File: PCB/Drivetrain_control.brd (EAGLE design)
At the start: 94 x 109.9 mm, 49 parts, among them IC1 LM358N, J1 SSW-110-02-G-S, J2 SSW-110-02-G-S, J3 SSW-110-02-G-S, J4 SSW-110-02-G-S, J5 SSW-110-02-G-S, J6 SSW-110-02-G-S, J7 SSW-110-02-G-S, J8 SSW-110-02-G-S, Q1 220mA/50V/3.5Ω, Q10 100V/17A, Q2 100V/17A, Q6 100V/17A, Q7 100V/17A, Q8 100V/17A, Q9 100V/17A

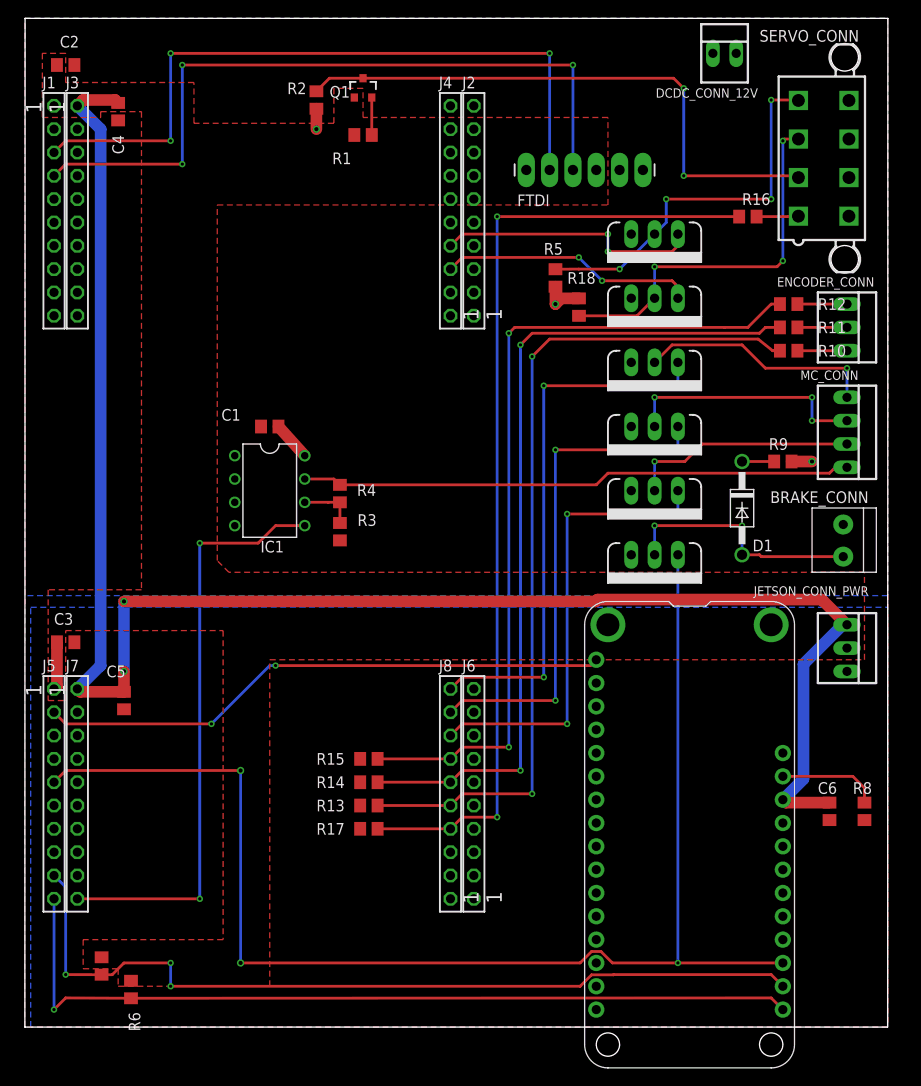
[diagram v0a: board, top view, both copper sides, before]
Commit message: Changed Size now, 100mm x 100mm, Stil Version 1.0
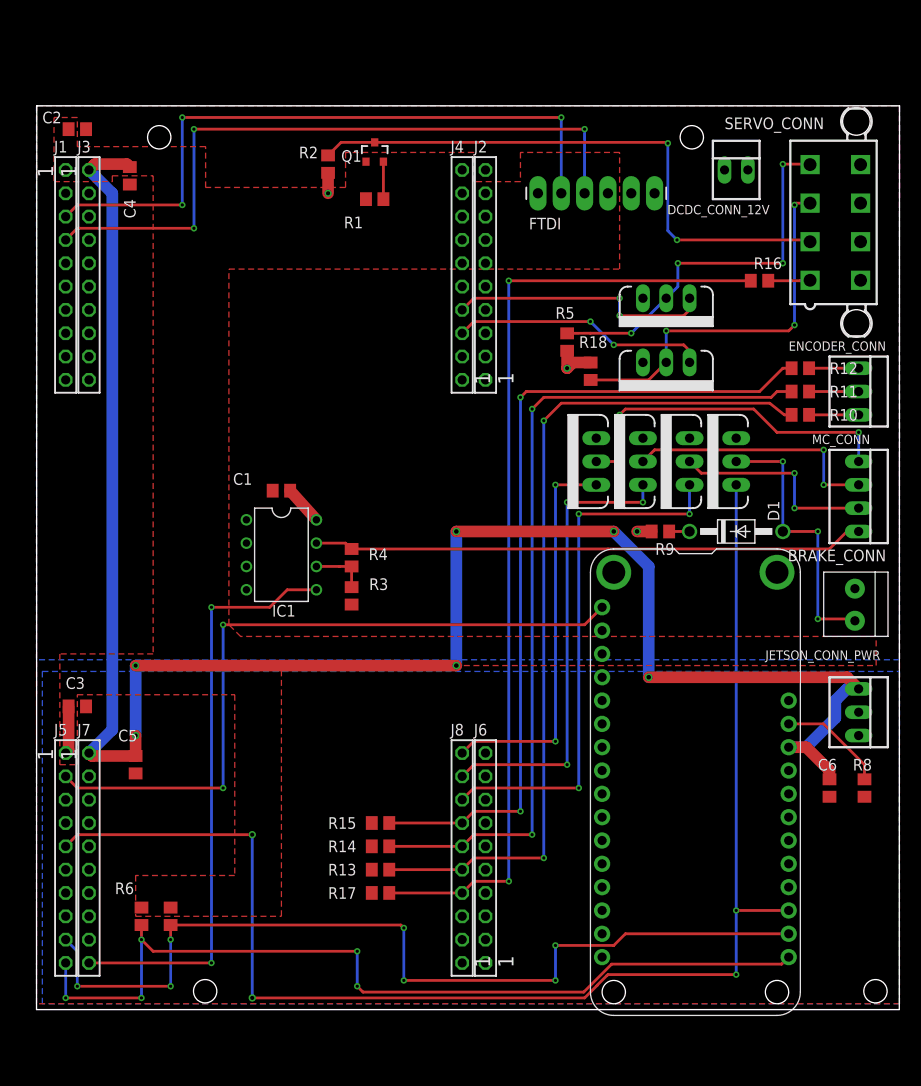
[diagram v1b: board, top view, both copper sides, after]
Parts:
- moved R9 15.4 mm to (68.6, 52.1), turned to 180 degrees
- moved Q10 13.5 mm to (76.8, 59.7), turned to 90 degrees
- moved DCDC_CONN_12V 12.8 mm to (76.8, 91.4)
- moved Q9 12.5 mm to (61.6, 59.7), turned to 90 degrees
- moved R7 9.26 mm to (15.2, 10.2)
- moved R6 8.06 mm to (12.1, 10.2)
- moved Q2 7.10 mm to (69.2, 70.5)
- moved Q6 7.10 mm to (69.2, 77.5)
- moved R13 7.10 mm to (38.1, 15.2)
- moved J2 7.10 mm to (49.5, 80.0)
- moved J4 7.10 mm to (47.0, 80.0)
- moved J6 7.10 mm to (49.5, 16.5)
- moved J8 7.10 mm to (47.0, 16.5)
- moved Q1 7.10 mm to (37.5, 93.3)
- moved R1 7.10 mm to (37.5, 88.3)
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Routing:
- net +5V: track 192.9 -> 210.8 mm, vias 2 -> 6
- net FS1_CTL: track 59.6 -> 43.1 mm, vias 3 -> 2
- net FEATHER_RESET: track 62.5 -> 77.5 mm
- net FS1_MC: track 26.0 -> 38.1 mm, vias 1 -> 3
- net REV_CTL: track 50.7 -> 58.3 mm
- net I2CSCLB: track 93.5 -> 99.9 mm, vias 3 -> 7
- net KILL_SIGNAL: track 146.3 -> 151.4 mm, vias 3 -> 4
- net SCIB_RX: track 76.7 -> 72.3 mm
- net FWD_CTL: track 55.1 -> 50.7 mm
- net SCIB_TX: track 79.3 -> 74.8 mm
- net I2CSDAB: track 92.5 -> 96.7 mm, vias 1 -> 5
- net BRAKE_SOLENOID: track 27.0 -> 30.1 mm, vias 2 -> 3
- net REV_MC: track 24.9 -> 22.8 mm, vias 1 -> 2
- net N$2: track 3.50 -> 2.22 mm
- net FWD_MC: track 26.7 -> 27.8 mm, vias 3 -> 2
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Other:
- board size 94 x 109.9 mm -> 94 x 98.4 mm
